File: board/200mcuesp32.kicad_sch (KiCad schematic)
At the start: 4 parts, among them U102 ESP32-S3-DEVKITC-1U-N8R2

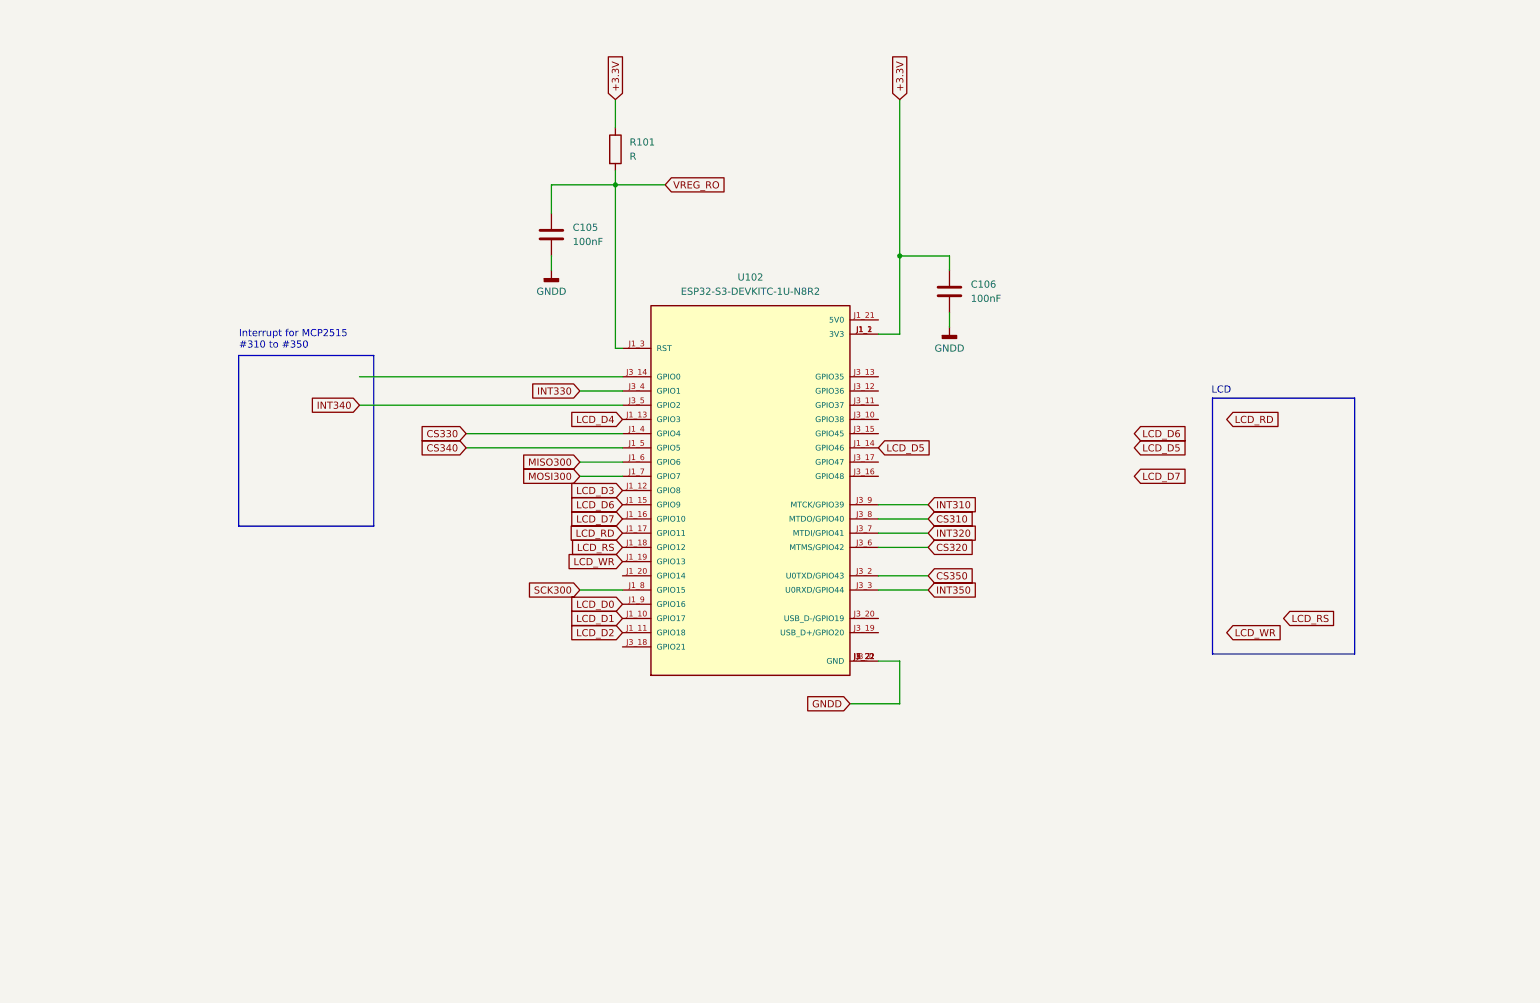
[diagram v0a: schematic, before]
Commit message: Added stl and skp files for 3D printing, changed ground planes and net names, exported schematics as pdf
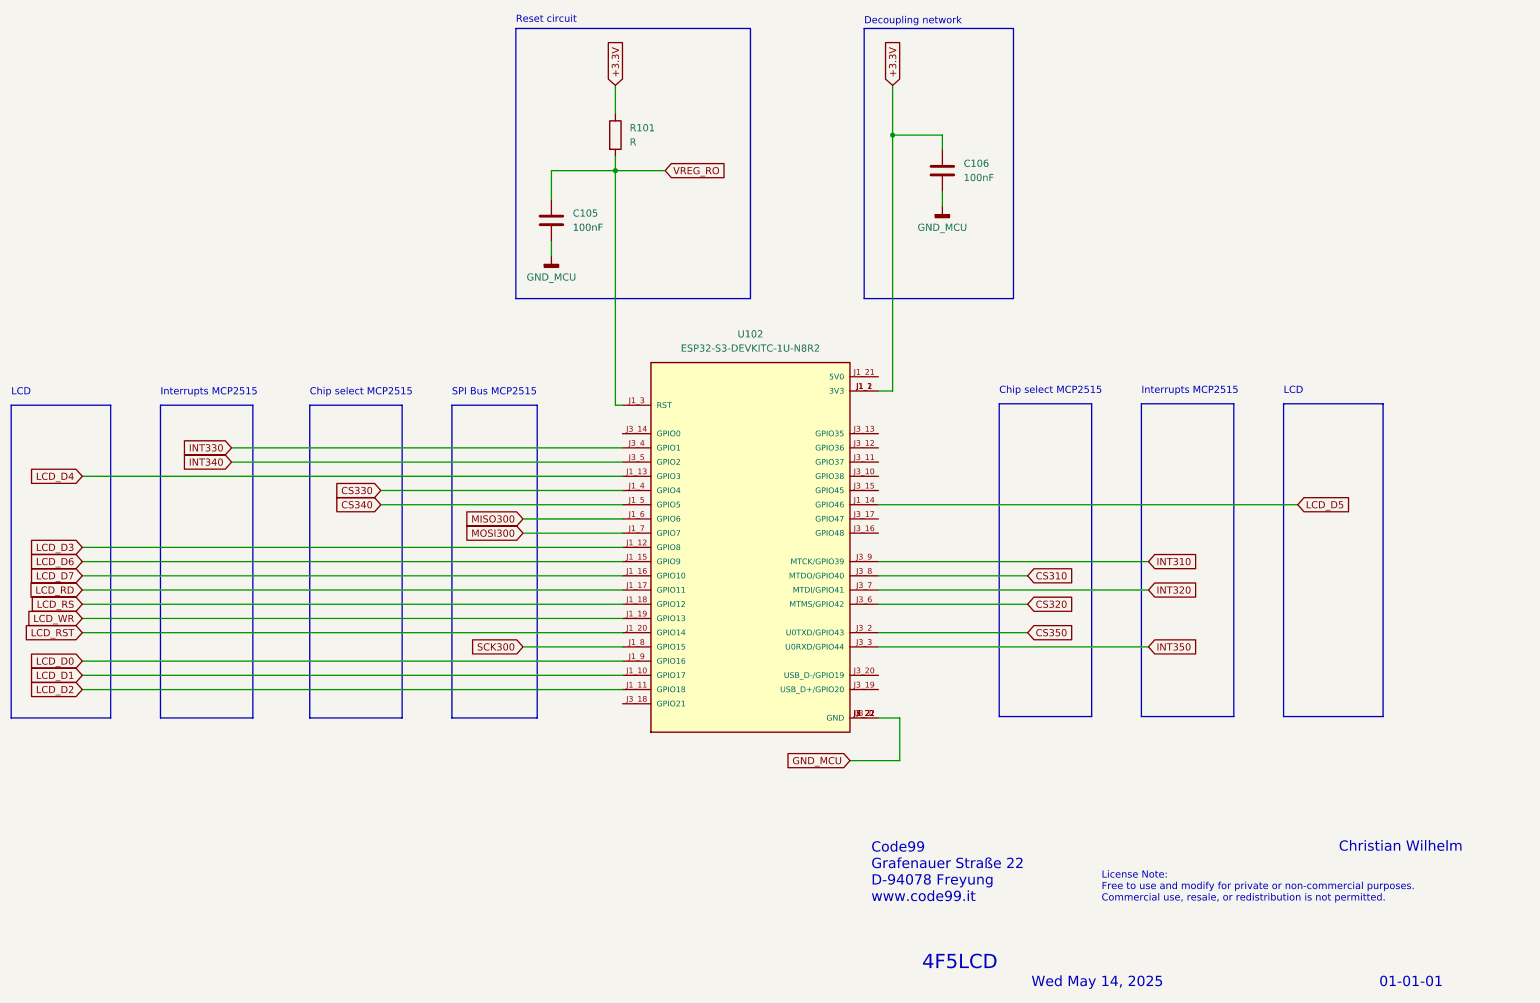
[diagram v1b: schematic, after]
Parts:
- C106: footprint (none) -> Capacitor_SMD:C_1206_3216Metric_Pad1.33x1.80mm_HandSolder
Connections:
- net LCD_RST: now reaches U102.J1_20 (GPIO14)
- net GNDD renamed GND_MCU
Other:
- note added: "01-01-01"
- note added: "4F5LCD"
- note added: "Chip select MCP2515"
- note added: "Christian Wilhelm"
- note added: "Code99 Grafenauer Straße 22 D-94078 Freyung www.code99.it"
- note added: "Decoupling network"
- note added: "Interrupts MCP2515"
- note added: "License Note: Free to use and modify for private or non-commercial purposes. Commercial use, resale, or redistribution is not permitted."
- note added: "Reset circuit"
- note added: "SPI Bus MCP2515"
- note added: "Wed May 14, 2025"
- note removed: "Interrupt for MCP2515 #310 to #350"
- moved on the sheet: C105, C106, R101, U102
